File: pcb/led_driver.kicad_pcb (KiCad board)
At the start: 2 copper layers, 30 x 30 mm, 41 parts, among them P1 POWER, P2 ICSP, Q1 DMP2305U, Q2 DMP2305U, SW1 UP, SW2 DOWN, U1 PIC16(L)F616-I/ST

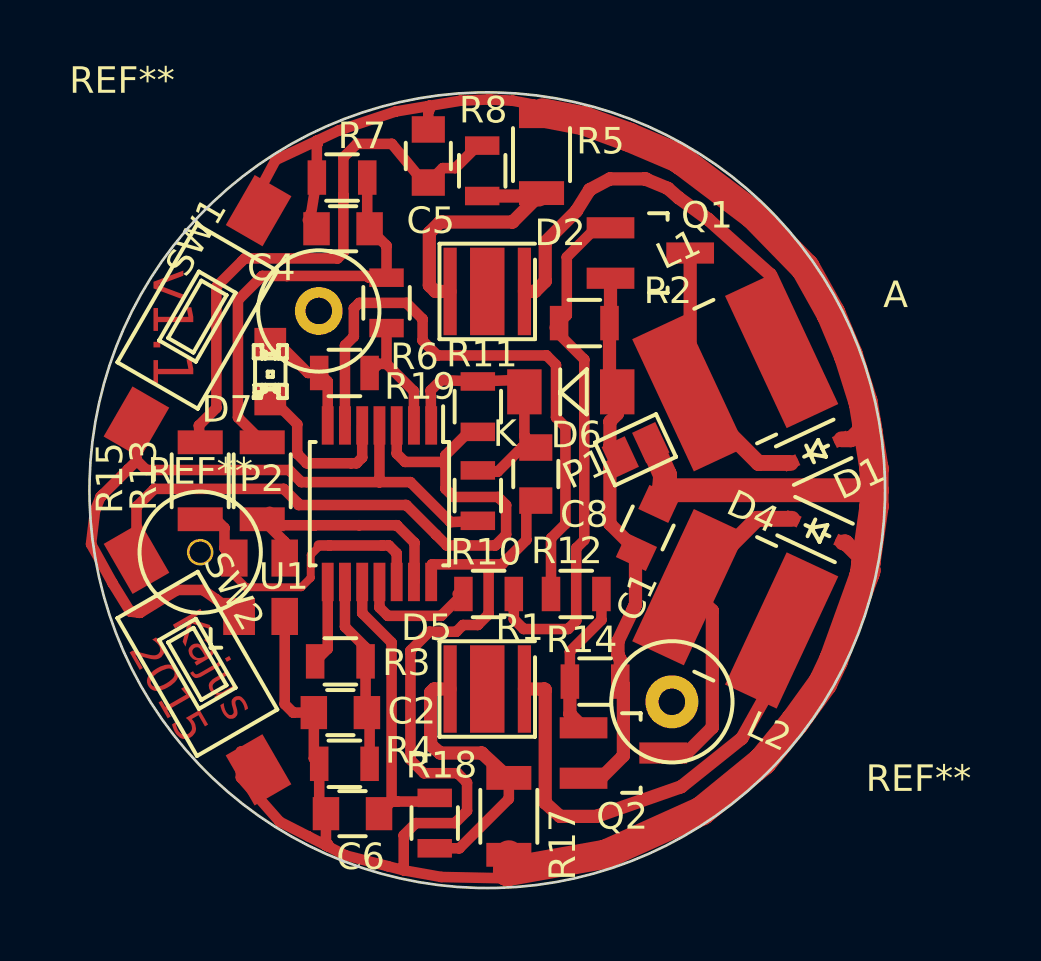
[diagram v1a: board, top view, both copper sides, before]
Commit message: Thermal vias added
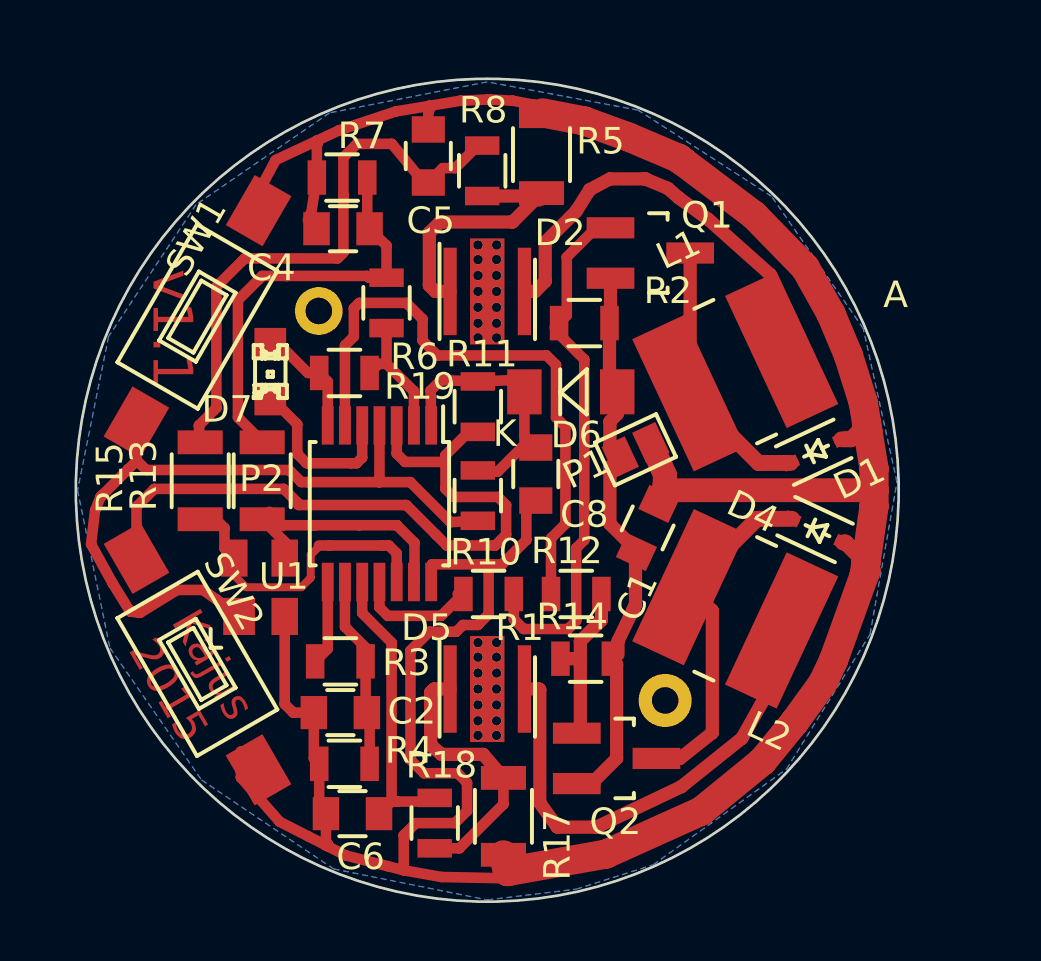
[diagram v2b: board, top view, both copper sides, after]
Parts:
- removed the REF** at (102.2, 99.9)
- REF**: moved to B.Cu
- moved R14 0.93 mm to (116.7, 103.9)
- moved Q2 0.33 mm to (117.9, 107.6)
- moved REF** 0.26 mm to (119.7, 105.5)
- moved R17 0.20 mm to (113.6, 109.8)
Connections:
- D2 pad 3: (no net) -> /HEATSINK
- D5 pad 3: (no net) -> /HEATSINK
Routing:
- net Net-(Q2-Pad1): track 5.99 -> 7.03 mm
- net VCC: track 21.8 -> 22.7 mm
- added copper zone on B.Cu, net /HEATSINK
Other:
- board size 30 x 30 mm -> 31 x 31 mm

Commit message: Cleanup, preparing for manufacturing
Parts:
- moved R5 1.13 mm to (116.0, 84.3), turned to 0 degrees
- moved Q1 0.61 mm to (118.6, 88.5)
- moved R8 0.61 mm to (112.9, 84.9), turned to 270 degrees
- moved D7 0.25 mm to (104.6, 93.2)
- moved REF** 0.23 mm to (106.5, 90.9)
- moved R2 0.18 mm to (116.8, 91.4)
- moved P1 0.16 mm to (118.5, 96.1), turned to 270 degrees
- moved R12 0.15 mm to (116.2, 101.4)
- moved SW2 0.11 mm to (102.2, 104.0)
- moved R19 0.10 mm to (107.6, 93.2)
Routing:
- net GND: track 125.3 -> 127.1 mm
- net VCC: track 22.7 -> 23.6 mm
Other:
- board size 31 x 31 mm -> 31.2 x 31.2 mm
- board text added: "+"
- board text added: "max 5,3V min 3V"
- board text added: "v1.2"
- board text removed: "v1.1"

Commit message: Cleanup before sending to seedstudio
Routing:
- net GND: track 127.1 -> 126.2 mm
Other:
- board text added: "DarkStar"

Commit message: Divider modified for higher stability and overcurrent protection on fw error
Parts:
- C2, C4: value 820n -> 1u
- R3, R6: value 100k -> 190k
- R4, R7: value 4k7 -> 5k6
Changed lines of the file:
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@@
     (links 96)
     (no_connects 0)
-    (area 96.642143 81.0694 131.449858 113.639601)
+    (area 97.370107 81.876107 128.689893 113.195893)
     (thickness 1.6)
     (drawings 8)
@@
       (effects (font (size 1 1) (thickness 0.15)))
     )
-    (fp_text value 820n (at 0 2.1 180) (layer F.Fab)
+    (fp_text value 1u (at 0 2.1 180) (layer F.Fab)
       (effects (font (size 1 1) (thickness 0.15)))
     )
@@
       (effects (font (size 1 1) (thickness 0.15)))
     )
-    (fp_text value 100k (at 0 2.1) (layer F.Fab)
+    (fp_text value 190k (at 0 2.1) (layer F.Fab)
       (effects (font (size 1 1) (thickness 0.15)))
     )
@@
       (effects (font (size 1 1) (thickness 0.15)))
     )
-    (fp_text value 4k7 (at 0 2.1 180) (layer F.Fab)
+    (fp_text value 5k6 (at 0 2.1 180) (layer F.Fab)
       (effects (font (size 1 1) (thickness 0.15)))
     )
@@
       (effects (font (size 1 1) (thickness 0.15)))
     )
-    (fp_text value 4k7 (at 0 2.1 180) (layer F.Fab)
+    (fp_text value 5k6 (at 0 2.1 180) (layer F.Fab)
       (effects (font (size 1 1) (thickness 0.15)))
     )
@@
       (effects (font (size 1 1) (thickness 0.15)))
     )
-    (fp_text value 820n (at 0 2.1 180) (layer F.Fab)
+    (fp_text value 1u (at 0 2.1 180) (layer F.Fab)
       (effects (font (size 1 1) (thickness 0.15)))
     )
@@
       (effects (font (size 0.8 0.8) (thickness 0.15)))
     )
-    (fp_text value 100k (at 0 2.1 90) (layer F.Fab)
-      (effects (font (size 1 1) (thickness 0.15)))
-    )
+    (fp_text value 190k (at 0 2.1 90) (layer F.Fab)
+      (effects (font (size 1 1) (thickness 0.15)))
+    )

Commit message: Fixed resistor not in E12
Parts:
- R3, R6: value 190k -> 180k
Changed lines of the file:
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@@
-(kicad_pcb (version 4) (host pcbnew "(2015-11-29 BZR 6336, Git 7b0d981)-product")
+(kicad_pcb (version 4) (host pcbnew 4.0.1-stable)
   (general
     (links 96)
     (no_connects 0)
-    (area 97.370107 81.876107 128.689893 113.195893)
+    (area 96.642143 81.0694 131.449858 113.639601)
     (thickness 1.6)
     (drawings 8)
@@
       (effects (font (size 1 1) (thickness 0.15)))
     )
-    (fp_text value 190k (at 0 2.1) (layer F.Fab)
+    (fp_text value 180k (at 0 2.1) (layer F.Fab)
       (effects (font (size 1 1) (thickness 0.15)))
     )
@@
       (effects (font (size 0.8 0.8) (thickness 0.15)))
     )
-    (fp_text value 190k (at 0 2.1 90) (layer F.Fab)
-      (effects (font (size 1 1) (thickness 0.15)))
-    )
+    (fp_text value 180k (at 0 2.1 90) (layer F.Fab)
+      (effects (font (size 1 1) (thickness 0.15)))
+    )
